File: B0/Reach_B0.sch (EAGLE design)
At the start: 184 parts, among them IC1 TMC2100-LA, IC10 74AHC1G126DCK, IC11 74AHC1G126DCK, IC18 74AHC1G126DCK, IC2 TMC2100-LA, IC3 74AHC1G126DCK, IC4 74AHC1G126DCK, IC5 74AHC1G126DCK, IC6 74AHC1G126DCK, IC7 74AHC1G126DCK, IC8 TMC2100-LA, IC9 74AHC1G126DCK, P8 F-2X23-, P9 F-2X23-, Q2 AON6758, Q3 AON6758, U1 SN74AHC595PW, U10 RT8268, U11 PCA9685PW, U18 CAT24C256, U2 SN74AHC595PW, U3 MCP9600, U4 MCP9600, U5 MCP9600, U6 MCP9600, U7 SN74AHC595PW, X1 22-05-7028-02, X11 22-05-7028-02, X14 22-05-7048-04, X2 MSTBA4, X21 MSTBA2, X3 MSTBA2, X4 22-05-7028-02, X5 22-05-7028-02, X6 22-05-7048-04, X7 22-05-7028-02, X8 22-05-7048-04, X9 22-05-7028-02

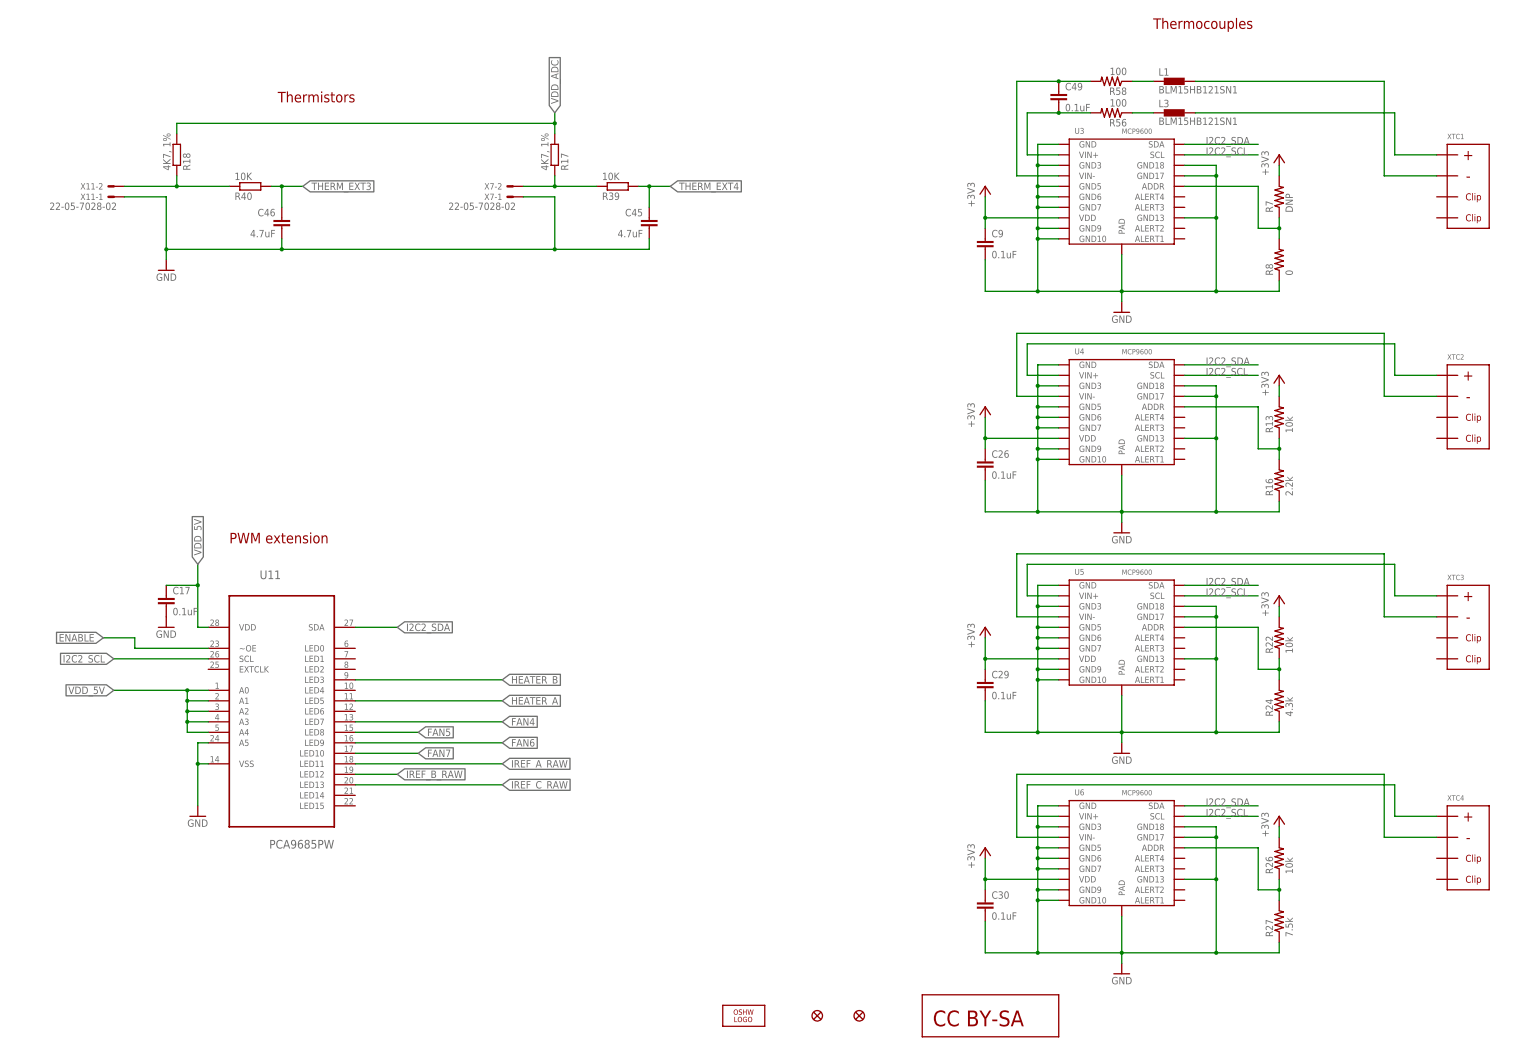
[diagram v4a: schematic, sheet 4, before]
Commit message: thermocouple layout complete
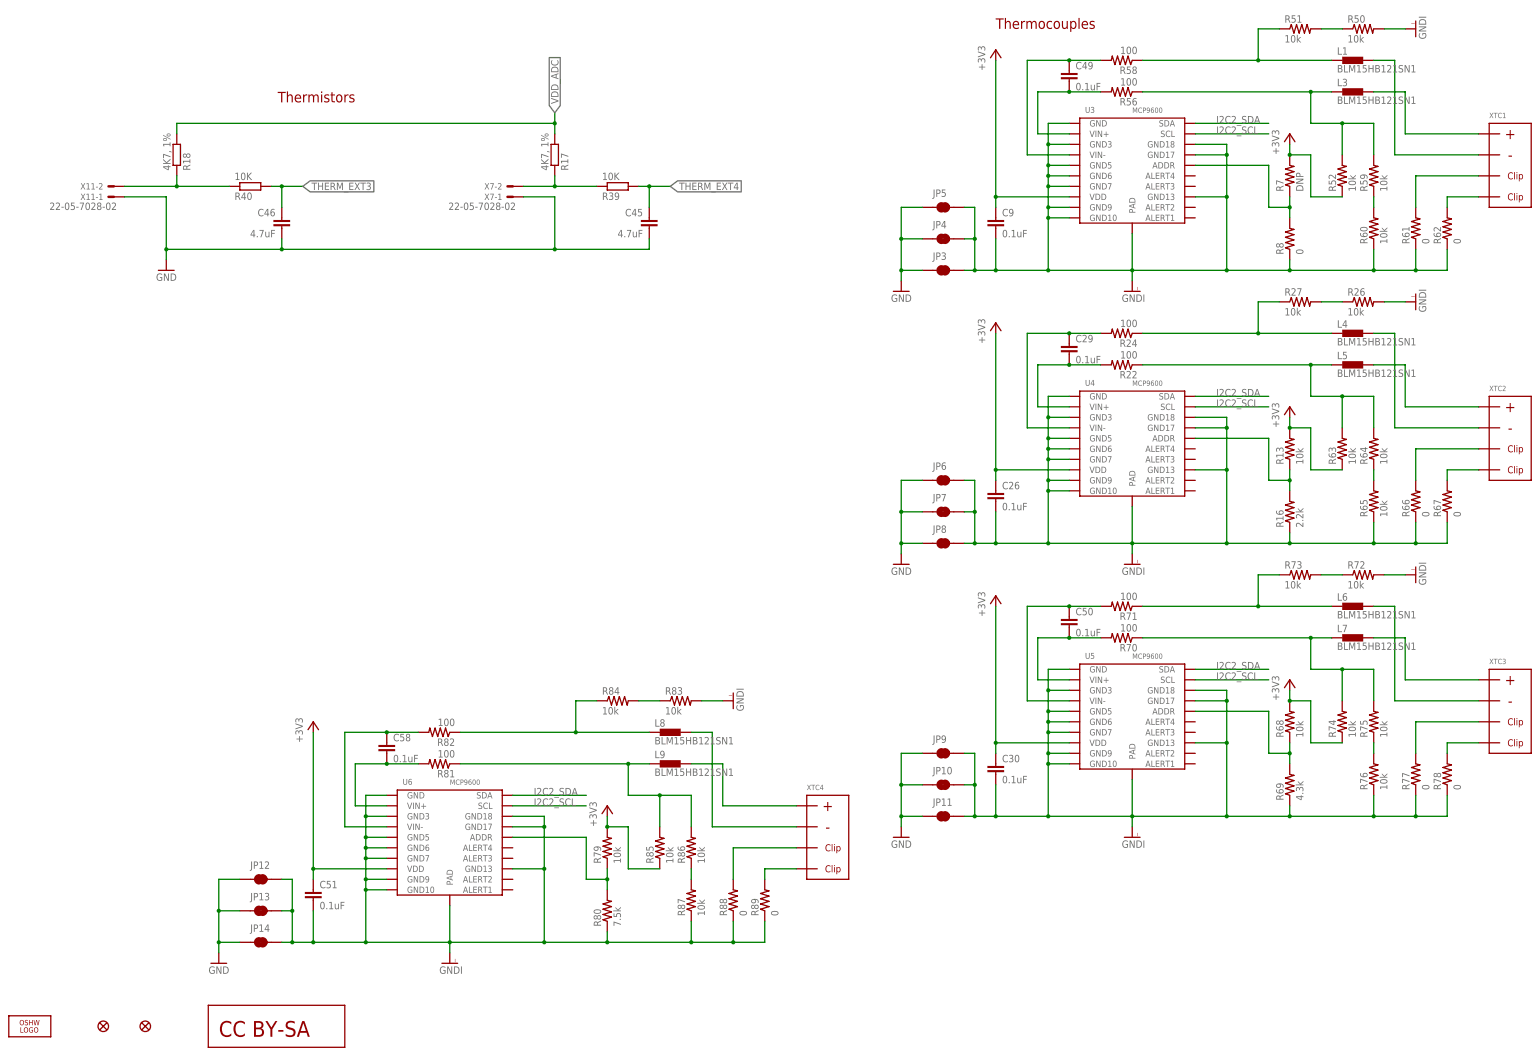
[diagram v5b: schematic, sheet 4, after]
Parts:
- added C50, C51, C58: 0.1uF, rcl:C-EUC0402
- added JP10, JP11, JP12, JP13, JP14, JP3, JP4, JP5, JP6, JP7, JP8, JP9: JUMPER-PAD-2-NC_BY_TRACE, SparkFun-PassivesNEW:JUMPER-PAD-2-NC_BY_TRACE
- added L4, L5, L6, L7, L8, L9: BLM15HB121SN1, inductors:BLM15HB121SN1
- added R50, R51, R52, R59, R60, R63, R64, R65, R72, R73, R74, R75, R76, R83, R84, R85, R86, R87: 10k, SparkFun-Resistors:RESISTOR0805-RES
- added R61, R62, R66, R67, R77, R78, R88, R89: 0, SparkFun-Resistors:RESISTOR0805-RES
- added R68, R79: 10k, SparkFun-Resistors:RESISTOR0402-RES
- added R69: 4.3k, SparkFun-Resistors:RESISTOR0402-RES
- added R70, R71, R81, R82: 100, SparkFun-Resistors:RESISTOR0402-RES
- added R80: 7.5k, SparkFun-Resistors:RESISTOR0402-RES
- R22: value 10k -> 100
- R24: value 4.3k -> 100
- R26: device SparkFun-Resistors:RESISTOR0402-RES -> SparkFun-Resistors:RESISTOR0805-RES
- R27: value 7.5k -> 10k; device SparkFun-Resistors:RESISTOR0402-RES -> SparkFun-Resistors:RESISTOR0805-RES
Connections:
- removed net N$41 (its old number): U4.VIN-, XTC2.P$2
- new net ENABLE_B: IC2.DRV_ENN_CFG6, IC7A.O
- new net GNDI: C26.2, C30.2, C51.2, C9.2, JP10.2, JP11.2, JP12.2, JP13.2, JP14.2, JP3.2, JP4.2, JP5.2, JP6.2, JP7.2, JP8.2, JP9.2, R16.1, R26.2, R50.2, R60.1, R61.1, R62.1, R65.1, R66.1, R67.1, R69.1, R72.2, R76.1, R77.1, R78.1, R8.1, R80.1, R83.2, R87.1, R88.1, R89.1, U3.GND, U3.GND10, U3.GND13, U3.GND17, U3.GND18, U3.GND3, U3.GND5, U3.GND6, U3.GND7, U3.GND9, U3.PAD, U4.GND, U4.GND10, U4.GND13, U4.GND17, U4.GND18, U4.GND3, U4.GND5, U4.GND6, U4.GND7, U4.GND9, U4.PAD, U5.GND, U5.GND10, U5.GND13, U5.GND17, U5.GND18, U5.GND3, U5.GND5, U5.GND6, U5.GND7, U5.GND9, U5.PAD, U6.GND, U6.GND10, U6.GND13, U6.GND17, U6.GND18, U6.GND3, U6.GND5, U6.GND6, U6.GND7, U6.GND9, U6.PAD
- new net N$123: L8.2, XTC4.P$2
- new net N$124: R79.1, R80.2, U6.ADDR
- new net N$125: L9.1, R81.1, R85.2, R86.2
- new net N$126: C58.2, R81.2, U6.VIN+
- new net N$128: C58.1, R82.2, U6.VIN-
- new net N$130: L9.2, XTC4.P$1
- new net N$131: L8.1, R82.1, R84.1
- new net N$132: R83.1, R84.2
- new net N$133: R86.1, R87.2
- new net N$134: R88.2, XTC4.P$3
- new net N$135: R89.2, XTC4.P$4
- new net N$42: L5.1, R22.1, R63.2, R64.2
- new net N$51: R61.2, XTC1.P$3
- new net N$73: R62.2, XTC1.P$4
- new net N$75: R59.1, R60.2
- new net N$76: R66.2, XTC2.P$3
- new net N$77: R67.2, XTC2.P$4
- new net N$87: L6.2, XTC3.P$2
- new net N$88: R68.1, R69.2, U5.ADDR
- new net N$89: L7.1, R70.1, R74.2, R75.2
- new net N$9: R50.1, R51.2
- new net N$90: C50.2, R70.2, U5.VIN+
- new net N$91: C50.1, R71.2, U5.VIN-
- new net N$92: L7.2, XTC3.P$1
- new net N$93: L6.1, R71.1, R73.1
- new net N$94: R72.1, R73.2
- new net N$95: R75.1, R76.2
- new net N$97: R77.2, XTC3.P$3
- new net N$98: R78.2, XTC3.P$4
- net +3V3: now also C51.1, R52.1, R63.1, R68.2, R74.1, R79.2, R85.1; no longer C29.1, R22.2, R26.2
- net ENABLE_A: no longer IC2.DRV_ENN_CFG6, IC7A.O
- net GND: now also JP10.1, JP11.1, JP12.1, JP13.1, JP14.1, JP3.1, JP4.1, JP5.1, JP6.1, JP7.1, JP8.1, JP9.1; no longer C26.2, C29.2, C30.2, C9.2, R16.1, R24.1, R27.1, R8.1, U3.GND, U3.GND10, U3.GND13, U3.GND17, U3.GND18, U3.GND3, U3.GND5, U3.GND6, U3.GND7, U3.GND9, U3.PAD, U4.GND, U4.GND10, U4.GND13, U4.GND17, U4.GND18, U4.GND3, U4.GND5, U4.GND6, U4.GND7, U4.GND9, U4.PAD, U5.GND, U5.GND10, U5.GND13, U5.GND17, U5.GND18, U5.GND3, U5.GND5, U5.GND6, U5.GND7, U5.GND9, U5.PAD, U6.GND, U6.GND10, U6.GND13, U6.GND17, U6.GND18, U6.GND3, U6.GND5, U6.GND6, U6.GND7, U6.GND9, U6.PAD
- net N$11: now also R52.2, R59.2
- net N$38: now also L4.2, XTC2.P$2; no longer U4.VIN+, XTC2.P$1
- net N$45: now also C29.2, R22.2, U4.VIN+; no longer U5.VIN+, XTC3.P$1
- net N$46: now also C29.1, R24.2, U4.VIN-; no longer U5.VIN-, XTC3.P$2
- net N$47: now also L5.2, XTC2.P$1; no longer R22.1, R24.2, U5.ADDR
- net N$48: now also L4.1, R24.1, R27.1; no longer U6.VIN+, XTC4.P$1
- net N$49: now also R26.1, R27.2; no longer U6.VIN-, XTC4.P$2
- net N$50: now also R64.1, R65.2; no longer R26.1, R27.2, U6.ADDR
- net N$72: now also R51.1
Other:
- moved on the sheet: C26, C29, C30, C49, C9, IC11, IC18, IC7, L1, L3, R13, R16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

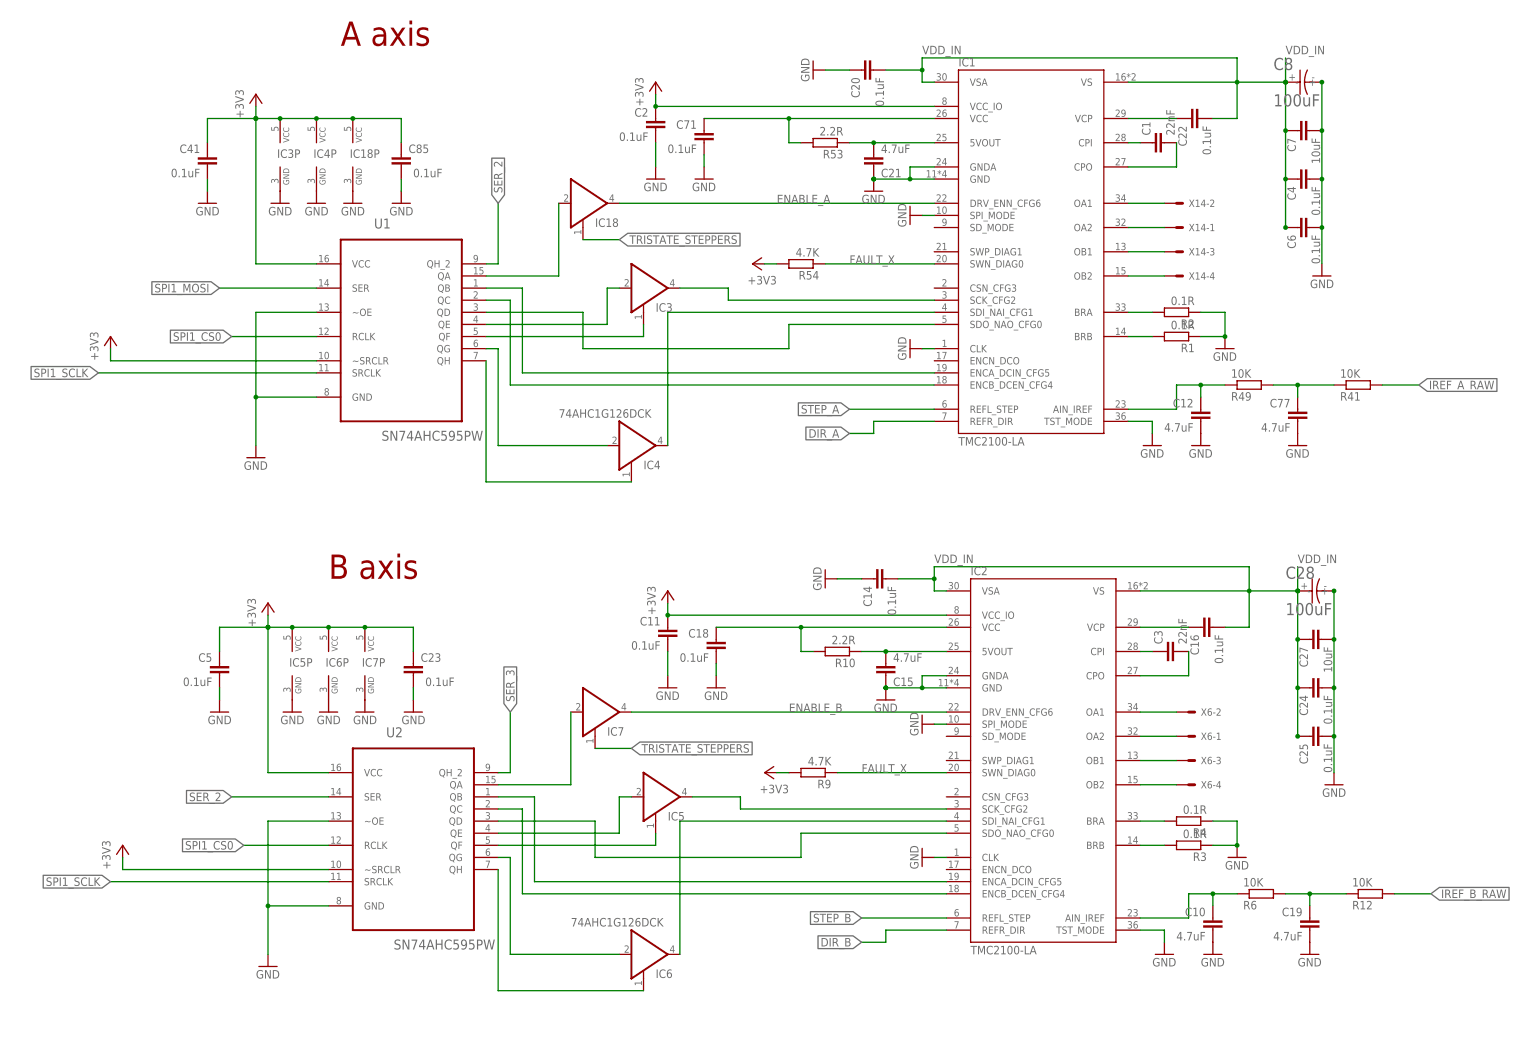
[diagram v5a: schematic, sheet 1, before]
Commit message: FETs added
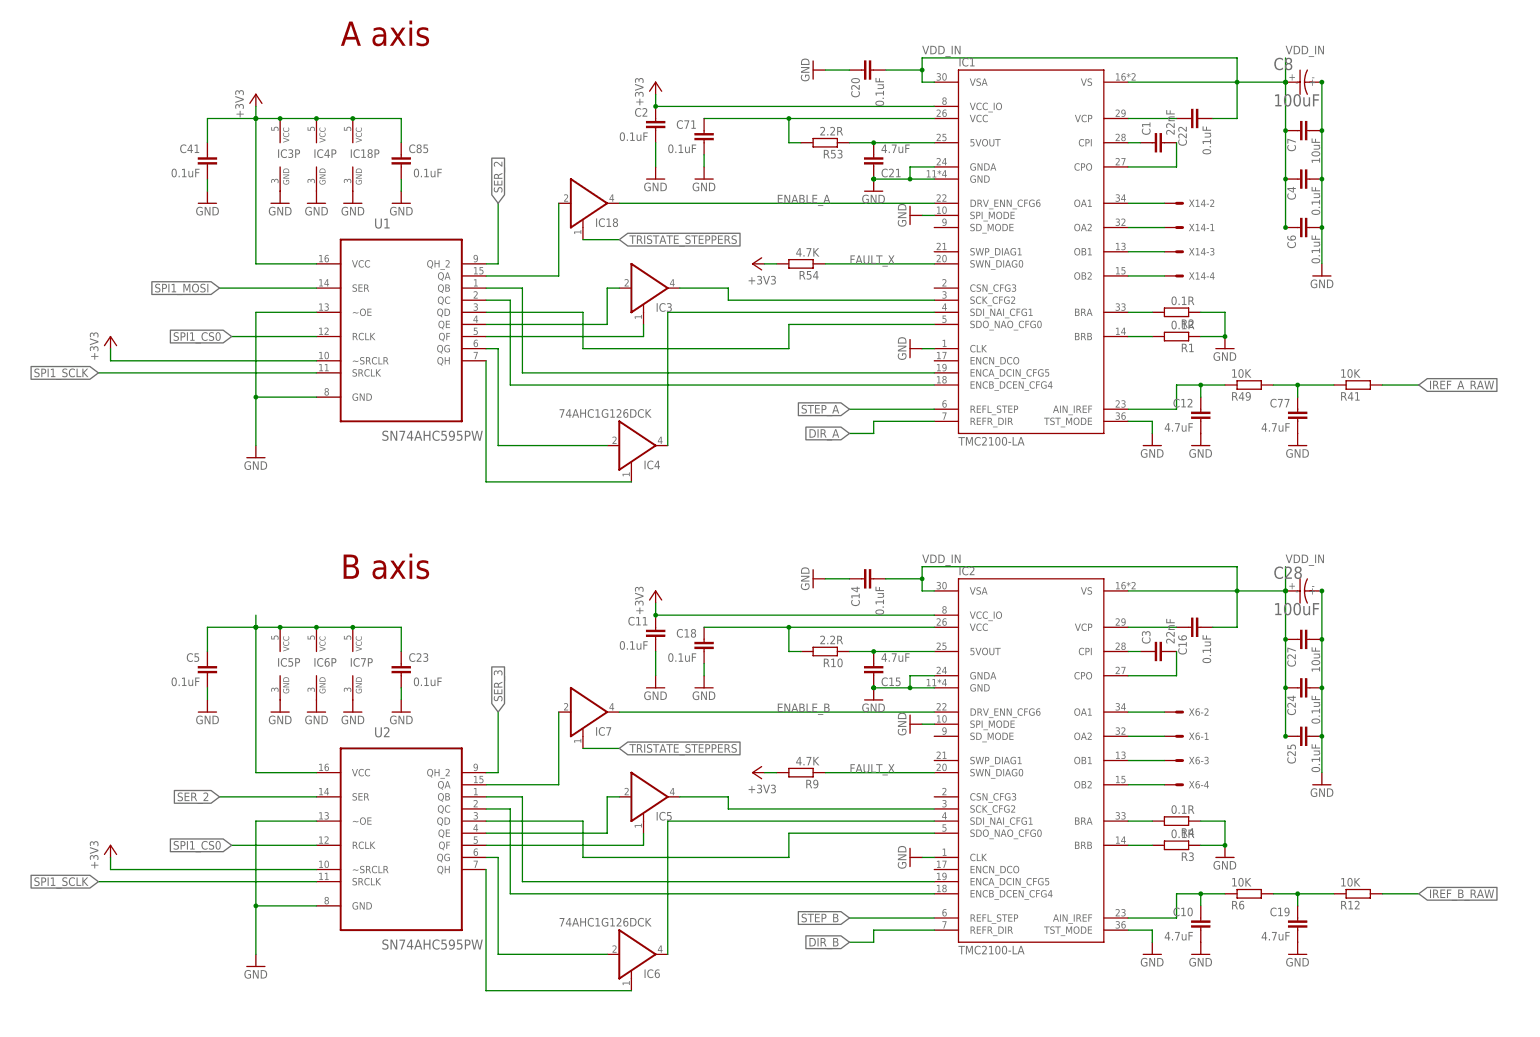
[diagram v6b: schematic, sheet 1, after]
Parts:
- removed LED7: blue, led:LEDCHIP-LED0603
- removed Q7: (no value), semicon-smd-ipc:NPN-TRANSISTOR_SOT23
- added LED2: blue, led:LEDCHIP-LED0603
- added Q1: (no value), semicon-smd-ipc:NPN-TRANSISTOR_SOT23
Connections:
- net IREF_X renamed IREF_A
- net IREF_X1 renamed IREF_B
- net IREF_X2 renamed IREF_C
- net X_A3 renamed B_A3
- net X_A4 renamed B_A4
- net X_A5 renamed C_A3
- net X_A6 renamed C_A4
- net X_B3 renamed B_B3
- net X_B4 renamed B_B4
- net X_B5 renamed C_B3
- net X_B6 renamed C_B4
- removed net N$114: LED7.C, Q5.C, X1-2.S
- removed net N$115: LED6.C, Q4.C, X5-2.S
- removed net N$116: LED5.C, Q7.C, X4-2.S
- removed net N$117: LED6.A, R20.1
- removed net N$118: LED7.A, R21.1
- new net N$78: LED2.A, R5.1
- new net N$79: LED5.C, Q4.C, X4-2.S
- new net N$80: LED5.A, R20.1
- new net N$81: LED6.C, Q5.C, X5-2.S
- new net N$82: LED6.A, R32.1
- new net N$900: U7.QH_2
- net FAN5: now also Q1.B, R19.2; no longer Q7.B, R33.2
- net FAN6: now also R21.2; no longer R32.2
- net FAN7: now also R33.2; no longer R5.2
- net GND: now also Q1.E, R19.1, R21.1; no longer Q7.E, R32.1, R5.1
- net N$12: now also LED2.C, Q1.C, X1-2.S; no longer LED5.A, R19.1
- net VDD_12V: now also R32.2, R5.2; no longer R19.2, R21.2
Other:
- moved on the sheet: C10, C11, C14, C15, C16, C18, C19, C23, C24, C25, C27, C28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

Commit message: Add files via upload
Changed pinout to make layout simpler
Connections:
- net DIR_A: now also P9.29; no longer P9.17
- net DIR_B: now also P9.21; no longer P9.26
- net DIR_C: now also P9.17; no longer P9.29
- net HEATER_A: now also U11.LED3; no longer U11.LED5
- net HEATER_B: now also U11.LED5; no longer U11.LED3
- net SPI1_CS0: now also P9.27
- net STEP_A: now also P9.26; no longer P9.15
- net STEP_C: now also P9.15; no longer P9.21
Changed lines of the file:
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@@
 <?xml version="1.0" encoding="utf-8"?>
 <!DOCTYPE eagle SYSTEM "eagle.dtd">
-<eagle version="8.1.0">
+<eagle version="8.1.1">
 <drawing>
 <settings>
@@
 <setting verticaltext="up"/>
 </settings>
-<grid distance="0.1" unitdist="inch" unit="inch" style="lines" multiple="1" display="no" altdistance="0.01" altunitdist="inch" altunit="inch"/>
+<grid distance="0.1" unitdist="inch" unit="mm" style="lines" multiple="1" display="no" altdistance="0.01" altunitdist="inch" altunit="inch"/>
 <layers>
 <layer number="1" name="Top" color="4" fill="1" visible="no" active="no"/>
@@
 <segment>
 <label x="157.48" y="53.34" size="1.778" layer="95" rot="R180" xref="yes"/>
-<wire x1="165.1" y1="53.34" x2="157.48" y2="53.34" width="0.1524" layer="91"/>
+<pinref part="P9" gate="G$1" pin="27"/>
+<wire x1="157.48" y1="53.34" x2="165.1" y2="53.34" width="0.1524" layer="91"/>
 </segment>
 </net>
@@
 <net name="DIR_B" class="0">
 <segment>
-<pinref part="P9" gate="G$1" pin="26"/>
-<wire x1="180.34" y1="55.88" x2="187.96" y2="55.88" width="0.1524" layer="91"/>
-<label x="187.96" y="55.88" size="1.778" layer="95" xref="yes"/>
+<label x="132.08" y="60.96" size="1.778" layer="95" rot="R180" xref="yes"/>
+<pinref part="P9" gate="G$1" pin="21"/>
+<wire x1="165.1" y1="60.96" x2="132.08" y2="60.96" width="0.1524" layer="91"/>
 </segment>
 </net>
@@
 <net name="STEP_A" class="0">
 <segment>
-<pinref part="P9" gate="G$1" pin="15"/>
-<label x="154.94" y="68.58" size="1.778" layer="95" rot="R180" xref="yes"/>
-<wire x1="165.1" y1="68.58" x2="154.94" y2="68.58" width="0.1524" layer="91"/>
+<label x="193.04" y="55.88" size="1.778" layer="95" xref="yes"/>
+<pinref part="P9" gate="G$1" pin="26"/>
+<wire x1="180.34" y1="55.88" x2="193.04" y2="55.88" width="0.1524" layer="91"/>
 </segment>
 </net>
 <net name="DIR_A" class="0">
 <segment>
-<pinref part="P9" gate="G$1" pin="17"/>
-<label x="129.54" y="66.04" size="1.778" layer="95" rot="R180" xref="yes"/>
-<wire x1="165.1" y1="66.04" x2="129.54" y2="66.04" width="0.1524" layer="91"/>
+<label x="134.62" y="50.8" size="1.778" layer="95" rot="R180" xref="yes"/>
+<pinref part="P9" gate="G$1" pin="29"/>
+<wire x1="134.62" y1="50.8" x2="165.1" y2="50.8" width="0.1524" layer="91"/>
 </segment>
 </net>
@@
 <net name="DIR_C" class="0">
 <segment>
-<pinref part="P9" gate="G$1" pin="29"/>
-<wire x1="165.1" y1="50.8" x2="129.54" y2="50.8" width="0.1524" layer="91"/>
-<label x="129.54" y="50.8" size="1.778" layer="95" rot="R180" xref="yes"/>
+<label x="129.54" y="66.04" size="1.778" layer="95" rot="R180" xref="yes"/>
+<pinref part="P9" gate="G$1" pin="17"/>
+<wire x1="165.1" y1="66.04" x2="129.54" y2="66.04" width="0.1524" layer="91"/>
 </segment>
 </net>
 <net name="STEP_C" class="0">
 <segment>
-<pinref part="P9" gate="G$1" pin="21"/>
-<wire x1="165.1" y1="60.96" x2="129.54" y2="60.96" width="0.1524" layer="91"/>
-<label x="129.54" y="60.96" size="1.778" layer="95" rot="R180" xref="yes"/>
+<label x="149.86" y="68.58" size="1.778" layer="95" rot="R180" xref="yes"/>
+<pinref part="P9" gate="G$1" pin="15"/>
+<wire x1="165.1" y1="68.58" x2="149.86" y2="68.58" width="0.1524" layer="91"/>
 </segment>
 </net>
@@
 <net name="HEATER_B" class="0">
 <segment>
-<pinref part="U11" gate="A" pin="LED3"/>
-<wire x1="312.42" y1="99.06" x2="347.98" y2="99.06" width="0.1524" layer="91"/>
-<label x="347.98" y="99.06" size="1.778" layer="95" xref="yes"/>
+<label x="347.98" y="93.98" size="1.778" layer="95" xref="yes"/>
+<wire x1="312.42" y1="93.98" x2="347.98" y2="93.98" width="0.1524" layer="91"/>
+<pinref part="U11" gate="A" pin="LED5"/>
 </segment>
 </net>
 <net name="HEATER_A" class="0">
 <segment>
-<pinref part="U11" gate="A" pin="LED5"/>
-<wire x1="312.42" y1="93.98" x2="347.98" y2="93.98" width="0.1524" layer="91"/>
-<label x="347.98" y="93.98" size="1.778" layer="95" xref="yes"/>
+<label x="347.98" y="99.06" size="1.778" layer="95" xref="yes"/>
+<pinref part="U11" gate="A" pin="LED3"/>
+<wire x1="347.98" y1="99.06" x2="312.42" y2="99.06" width="0.1524" layer="91"/>
 </segment>
 </net>
